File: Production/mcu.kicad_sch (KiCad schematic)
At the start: 16 parts, among them J301 TC2030-NL, U301 CC2340R5MODA

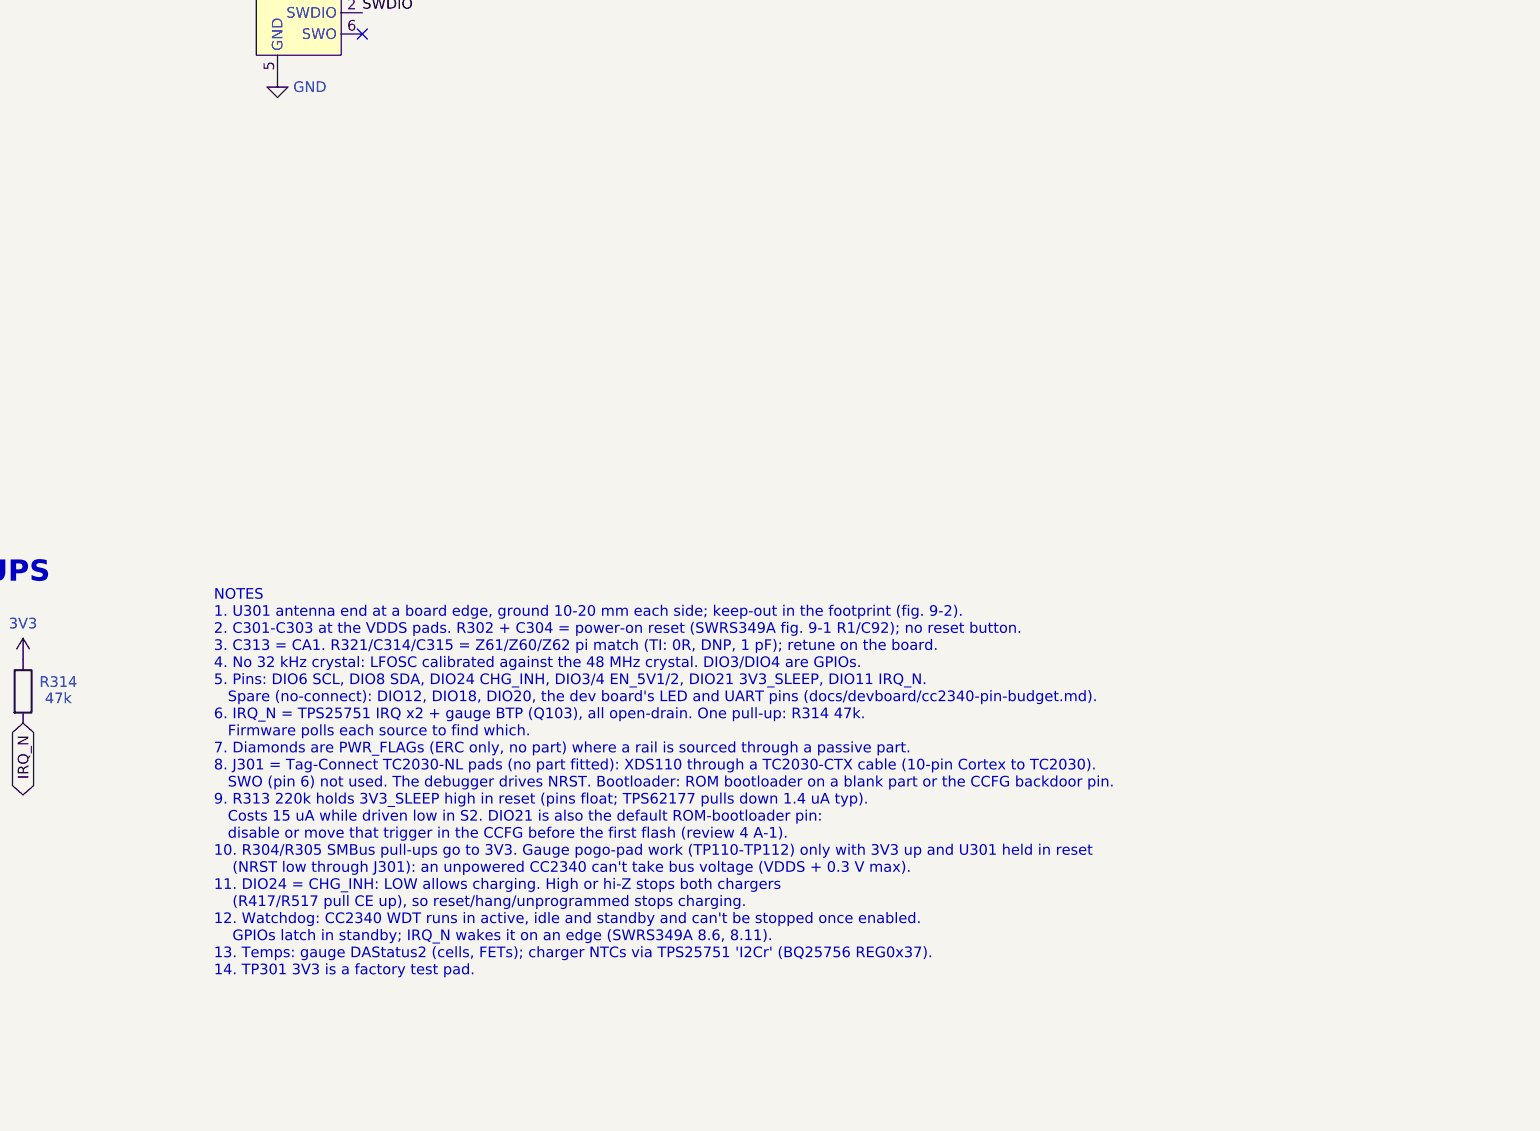
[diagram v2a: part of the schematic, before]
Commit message: Production P0 is the first build: gauge training access and tuning hedges
Dev board skipped. J302 = second TC2030-NL (GAUGE: SDA, CHG_INH, NRST, GND,
SCL) replacing the SMBus pogo pads; J113/J114 PACK_P/GND load pads for the
learning cycle; R118 4.7k + TP113 WAKE pad. Hedges: R444-R447 back as 0R
0402 gate links, DNP 0402 snubbers. Probe pads (1.0 mm) VBUS/PPHV/PP5V/REGN/
SW1/SW2/GND per port. docs/production/p0-bringup-and-training.md. Netlist
check passes; ERC known warnings only. Board/.kicad_pro (user WIP) not included.

Co-Authored-By: Claude Opus 5.5 <noreply@anthropic.com>
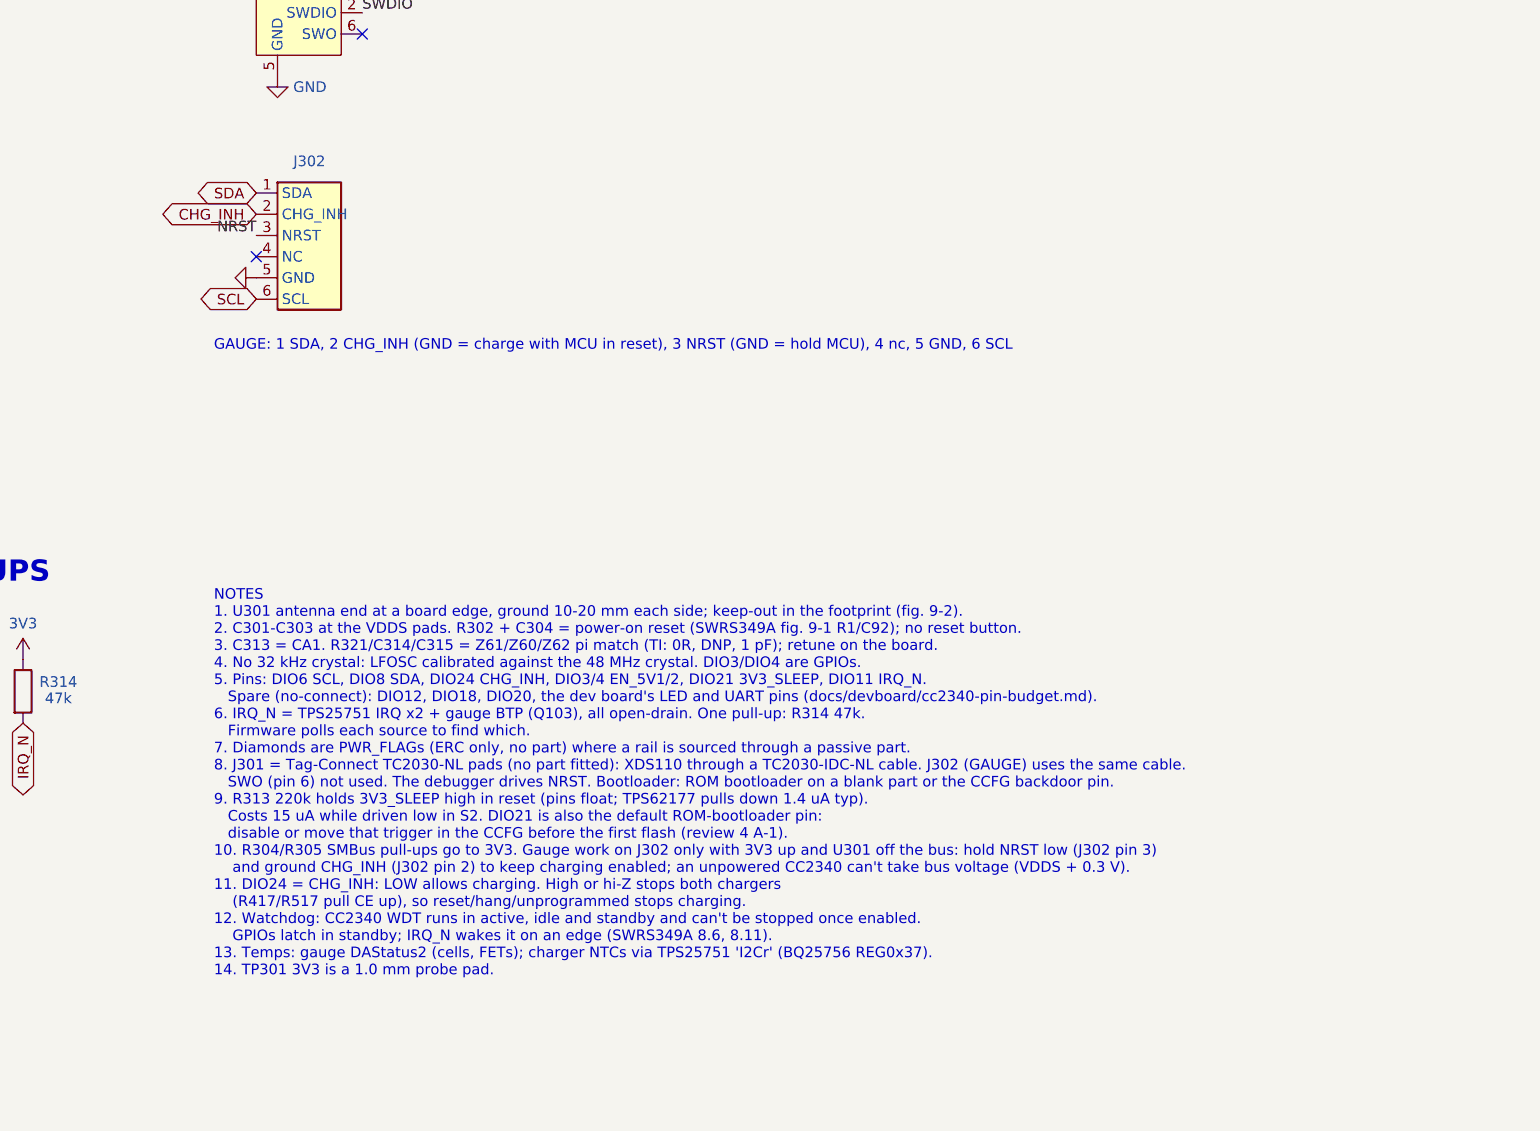
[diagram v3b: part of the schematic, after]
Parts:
- added J302: TC2030-NL GAUGE, Connector:Tag-Connect_TC2030-IDC-NL_2x03_P1.27mm_Vertical, symbol MonolithDev:TC2030_GAUGE
- TP301: footprint TestPoint:TestPoint_Pad_D1.5mm -> TestPoint:TestPoint_Pad_D1.0mm
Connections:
- net CHG_INH: now also J302.2 (CHG_INH)
- net GND: now also J302.5 (GND)
- net NRST: now also J302.3 (NRST)
- net SCL: now also J302.6 (SCL)
- net SDA: now also J302.1 (SDA)
- no-connect marks 4 -> 5
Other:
- note added: "GAUGE: 1 SDA, 2 CHG_INH (GND = charge with MCU in reset), 3 NRST (GND = hold MCU), 4 nc, 5 GND, 6 SCL"

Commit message: Production schematic P0: layout clean-up pass
New tools/layout_production.py (after make and tidy): block moves via
DevBoard/tools/move_region.py, then place_fields.py and check_overlaps.py.
Gauge: pack/NTC pads compacted, current sense and test/training pads moved up;
MCU: blocks regrouped, notes moved, J302 at 5.08 mm pin pitch; 3V3 Rail:
shared bulk and notes beside the rail; stale headings and index text fixed.
0 overlaps on all sheets; netlist check passes; ERC known warnings only.

Co-Authored-By: Claude Opus 5.5 <noreply@anthropic.com>
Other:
- note added: "3V3 PROBE PAD"
- note removed: "FACTORY TEST PAD"
- moved on the sheet: C301, C302, C303, C304, C313, C314, C315, R302, R304, R305, R313, R314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
